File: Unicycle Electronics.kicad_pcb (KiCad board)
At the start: 2 copper layers, 100 x 95 mm, 28 parts, among them J1 12V Input, J10 USB_C, J2 Tail Light, J3 BT1, J4 BT2, J5 BT3, J6 UART, J7 Tail Light, Q1 AO3402, SW1 PTS526SMG15SMTR2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

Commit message: PCB Revision 1
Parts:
- J7: value Tail Light -> Headlight
- moved J7 96.2 mm to (102.2, 122.5), turned to 90 degrees
- moved Q1 76.9 mm to (171.0, 41.5)
- moved C4 72.0 mm to (150.5, 41.0), turned to 90 degrees
- moved C2 66.4 mm to (148.0, 41.0), turned to 90 degrees
- moved C1 64.4 mm to (144.0, 41.5)
- moved J5 52.7 mm to (178.1, 67.0), turned to 90 degrees
- moved C3 49.6 mm to (146.5, 63.5), turned to 90 degrees
- moved R4 49.6 mm to (160.5, 117.5), turned to 180 degrees
- moved SW2 49.3 mm to (154.0, 60.0), turned to 180 degrees
- moved SW1 35.9 mm to (154.0, 67.0), turned to 180 degrees
- moved R8 33.9 mm to (160.5, 114.0)
- moved U3 33.2 mm to (145.5, 48.5)
- moved J10 31.4 mm to (174.2, 123.8)
- moved R3 31.0 mm to (170.0, 47.0), turned to 90 degrees
- moved J2 29.1 mm to (176.5, 41.0), turned to -90 degrees
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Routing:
- net +12V: track 0.00 -> 153.0 mm
- net GND: track 0.00 -> 112.2 mm, vias 0 -> 7
- net /DIM-: track 0.00 -> 96.2 mm
- net /USB-: track 0.00 -> 79.1 mm, vias 0 -> 2
- net /USB+: track 0.00 -> 76.4 mm, vias 0 -> 2
- net Net-(LED DRIVER1-PWM): track 0.00 -> 74.9 mm, vias 0 -> 2
- net +3.3V: track 0.00 -> 56.1 mm
- net /Head_Dimming: track 0.00 -> 41.1 mm, vias 0 -> 2
- net /BT1: track 0.00 -> 36.1 mm
- net /BOOT: track 0.00 -> 31.3 mm
- net /BT2: track 0.00 -> 29.1 mm
- net Net-(J7-Pin_2): track 0.00 -> 28.8 mm
- net Net-(U2-EN/CHIP_PU): track 0.00 -> 26.9 mm
- net /BT3: track 0.00 -> 22.8 mm
- net /RXD0: track 0.00 -> 17.8 mm
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- added copper zone on B.Cu, net GND

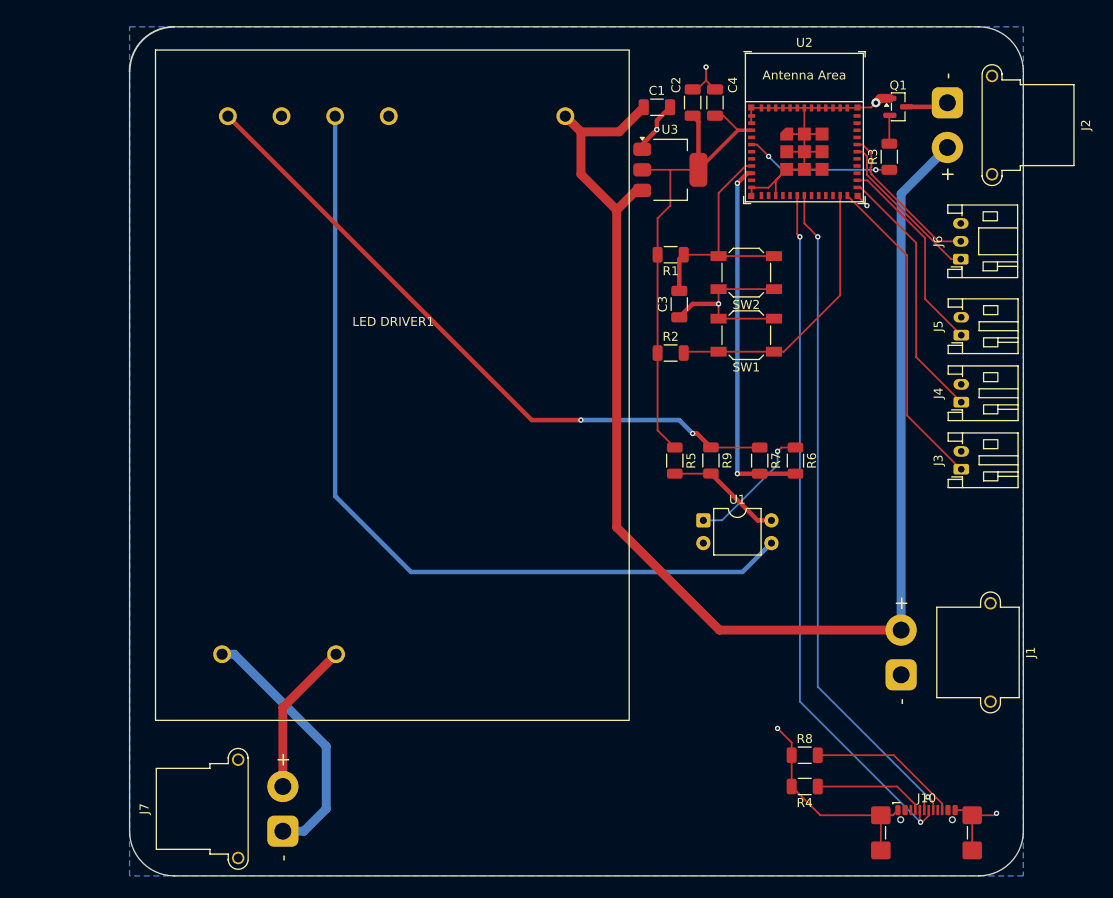
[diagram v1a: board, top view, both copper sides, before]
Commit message: Added mounting holes, updated footprints
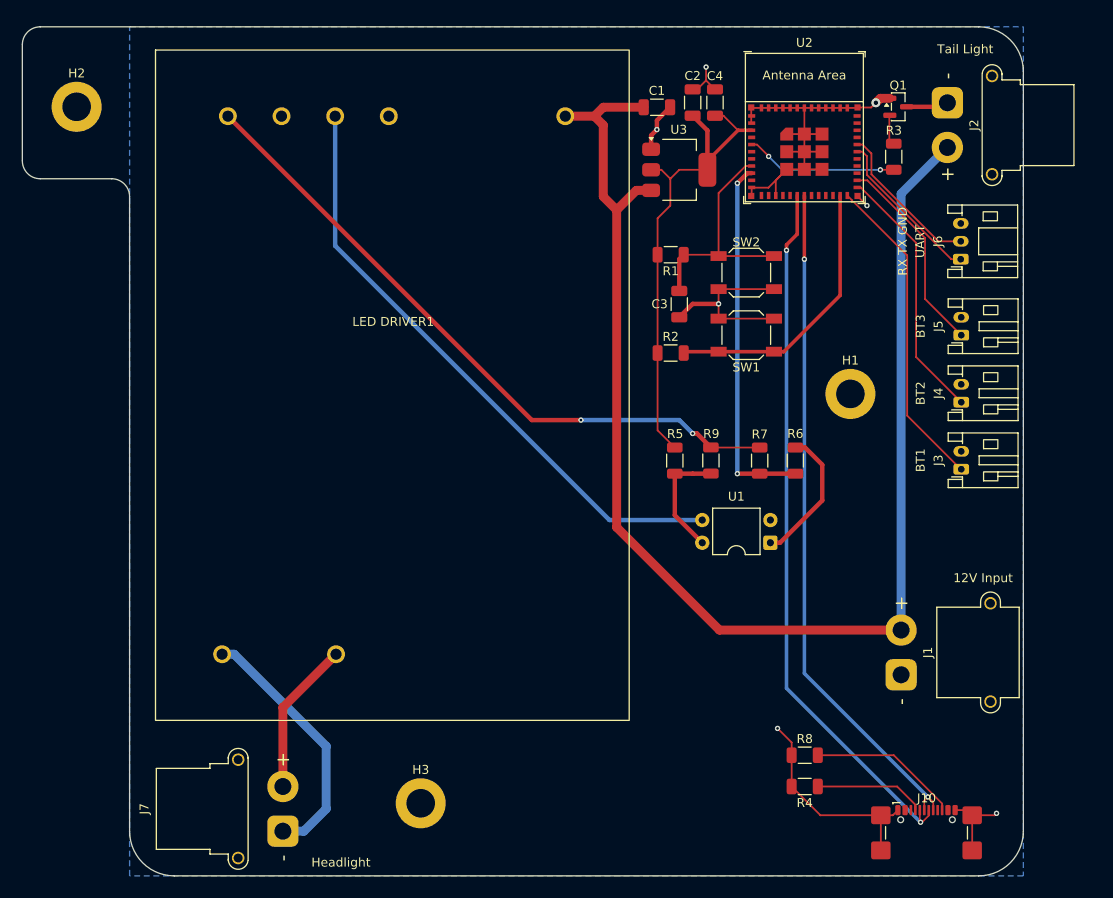
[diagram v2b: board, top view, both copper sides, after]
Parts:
- added H1: MountingHole, MountingHole:MountingHole_3.2mm_M3_DIN965_Pad, F.Cu at (165.7, 73.6)
- added H2: MountingHole, MountingHole:MountingHole_3.2mm_M3_DIN965_Pad, F.Cu at (79.1, 41.5)
- added H3: MountingHole, MountingHole:MountingHole_3.2mm_M3_DIN965_Pad, F.Cu at (117.6, 119.4)
- moved U1 7.91 mm to (156.7, 90.2), turned to 180 degrees
- moved U3 1.00 mm to (146.5, 48.5)
- moved R3 0.50 mm to (170.5, 47.0)
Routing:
- net /DIM-: track 96.2 -> 68.3 mm
- net Net-(R6-Pad1): track 14.6 -> 15.6 mm, vias 1 -> 0
- net /USB-: track 79.1 -> 80.1 mm
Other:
- board size 100 x 95 mm -> 112 x 95 mm
- board text added: "RX TX GND"

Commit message: pre mfg
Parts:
- moved H3 0.69 mm to (117.0, 119.0)
- moved H1 0.55 mm to (166.0, 74.0)
- moved H2 0.46 mm to (79.0, 41.0)
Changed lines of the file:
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@@
 	(footprint "MountingHole:MountingHole_3.2mm_M3_DIN965_Pad"
 		(layer "F.Cu")
-		(at 79.075 41.45)
+		(at 79 41)
 		(descr "Mounting Hole 3.2mm, M3, generated by kicad-footprint-generator mountinghole.py")
 		(tags "mountinghole M3 DIN965")
@@
 		(tags "resistor")
 		(property "Reference" "R7"
-			(at -2.943337 -0.00819 180)
+			(at -2.943337 -0.00819 0)
 			(layer "F.SilkS")
 			(effects
@@
 		(sheetname "/")
 		(sheetfile "Unicycle Electronics.kicad_sch")
-		(attr smd)
+		(attr smd dnp)
 		(fp_line
 			(start -0.727064 0.91)
@@
 	(footprint "MountingHole:MountingHole_3.2mm_M3_DIN965_Pad"
 		(layer "F.Cu")
-		(at 165.65 73.575)
+		(at 166 74)
 		(descr "Mounting Hole 3.2mm, M3, generated by kicad-footprint-generator mountinghole.py")
 		(tags "mountinghole M3 DIN965")
@@
 	(footprint "MountingHole:MountingHole_3.2mm_M3_DIN965_Pad"
 		(layer "F.Cu")
-		(at 117.575 119.375)
+		(at 117 119)
 		(descr "Mounting Hole 3.2mm, M3, generated by kicad-footprint-generator mountinghole.py")
 		(tags "mountinghole M3 DIN965")
@@
 		(polygon
 			(pts
-				(xy 85 32.5) (xy 185 32.5) (xy 185 127.5) (xy 85 127.5)
+				(xy 84.5 50) (xy 72.5 50) (xy 72.5 31.5) (xy 185 31.5) (xy 185 128) (xy 84.5 128)
 			)
 		)

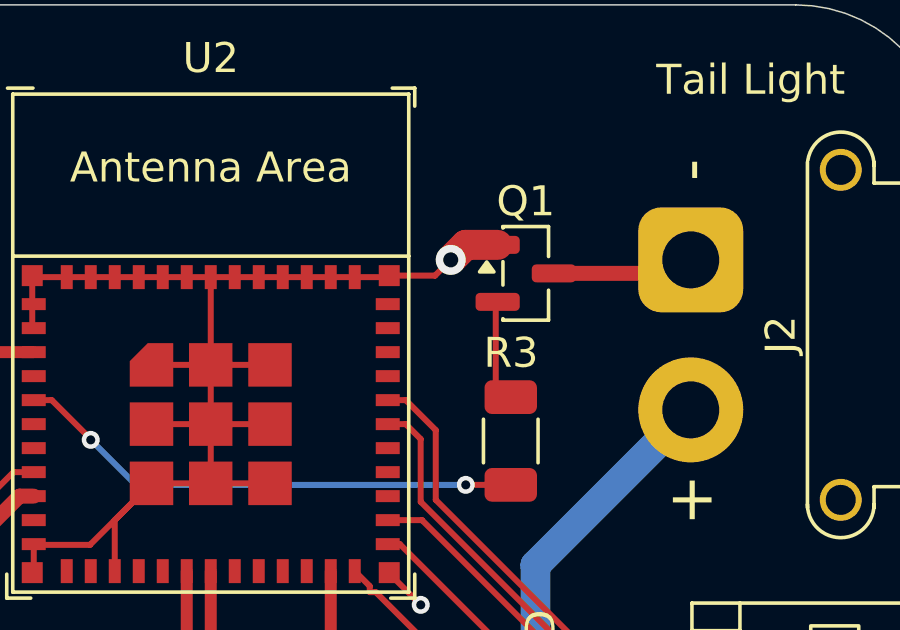
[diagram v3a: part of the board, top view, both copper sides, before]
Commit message: Fixed footprint and routing for tail light MOSFET
gate and source were switched, incorrect footprint :(
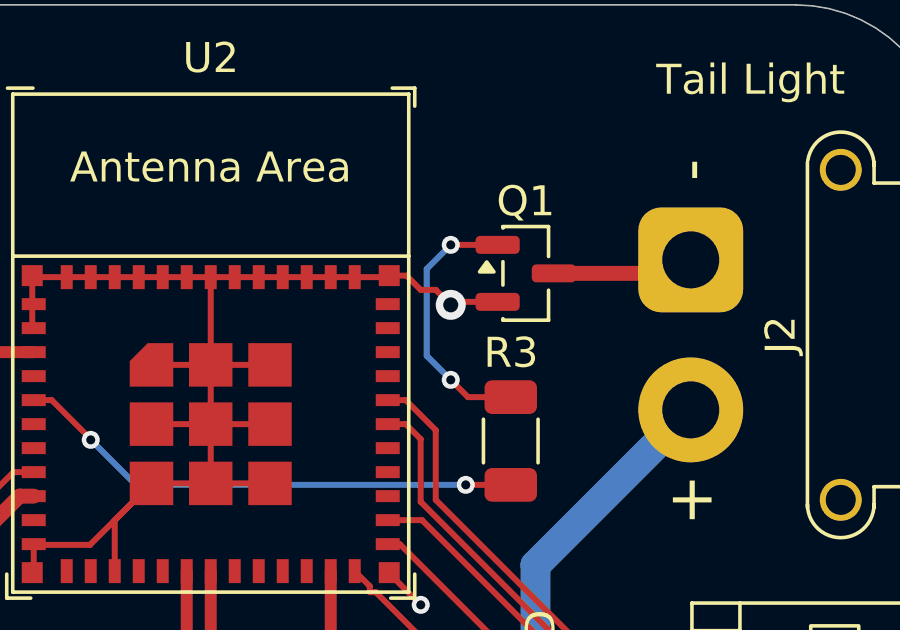
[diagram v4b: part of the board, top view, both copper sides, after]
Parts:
- Q1: footprint Package_TO_SOT_SMD:SOT-23 -> Unicycle:AO3402
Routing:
- net Net-(Q1-G): track 3.20 -> 8.96 mm, vias 0 -> 2
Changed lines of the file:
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@@
 		(sheetname "/")
 		(sheetfile "Unicycle Electronics.kicad_sch")
-		(attr smd dnp)
+		(attr smd)
 		(fp_line
 			(start -0.727064 0.91)
@@
 		)
 	)
-	(footprint "Package_TO_SOT_SMD:SOT-23"
+	(footprint "Unicycle:AO3402"
 		(layer "F.Cu")
 		(at 171 41.45)
@@
 		)
 		(pad "1" smd roundrect
-			(at -0.9375 -0.95)
+			(at -0.9375 0.95)
 			(size 1.475 0.6)
 			(layers "F.Cu" "F.Mask" "F.Paste")
@@
 		)
 		(pad "2" smd roundrect
-			(at -0.9375 0.95)
+			(at -0.9375 -0.95)
 			(size 1.475 0.6)
 			(layers "F.Cu" "F.Mask" "F.Paste")
@@
 	)
 	(segment
-		(start 170.0625 40.5)
-		(end 169 40.5)
-		(width 1)
-		(layer "F.Cu")
-		(net 1)
-	)
-	(segment
 		(start 162.29322 120.71822)
 		(end 169.05541 120.71822)
@@
 	)
 	(segment
-		(start 168.5 41)
-		(end 167.975 41.525)
+		(start 160.5 44.5)
+		(end 162.475 44.5)
 		(width 0.2)
 		(layer "F.Cu")
@@
 	)
 	(segment
-		(start 160.5 44.5)
-		(end 162.475 44.5)
+		(start 179.27541 124.64822)
+		(end 179.27541 120.71822)
 		(width 0.2)
 		(layer "F.Cu")
@@
 	)
 	(segment
-		(start 179.27541 124.64822)
-		(end 179.27541 120.71822)
+		(start 167.025 41.525)
+		(end 166.45 41.525)
 		(width 0.2)
 		(layer "F.Cu")
@@
 	)
 	(segment
-		(start 167.975 41.525)
-		(end 166.45 41.525)
-		(width 0.2)
-		(layer "F.Cu")
-		(net 1)
-	)
-	(segment
 		(start 160.5 46.475)
 		(end 160.5 48.45)
@@
 	)
 	(segment
+		(start 167.5 42)
+		(end 167.025 41.525)
+		(width 0.2)
+		(layer "F.Cu")
+		(net 1)
+	)
+	(segment
 		(start 148 63.5)
 		(end 150.9 63.5)
@@
 	)
 	(segment
-		(start 169 40.5)
-		(end 168.5 41)
-		(width 1)
-		(layer "F.Cu")
-		(net 1)
-	)
-	(segment
 		(start 154.55 43.225)
 		(end 154.6 43.275)
@@
 	)
 	(segment
+		(start 170.0625 42.4)
+		(end 168.6 42.4)
+		(width 0.2)
+		(layer "F.Cu")
+		(net 1)
+	)
+	(segment
 		(start 178.70041 120.14322)
 		(end 179.27541 120.71822)
@@
 	)
 	(segment
+		(start 170.0625 42.4)
+		(end 170 42.4625)
+		(width 0.2)
+		(layer "F.Cu")
+		(net 1)
+	)
+	(segment
 		(start 160.5 48.45)
 		(end 162.475 48.45)
@@
 	)
 	(segment
+		(start 168.5 42.5)
+		(end 168 42)
+		(width 0.2)
+		(layer "F.Cu")
+		(net 1)
+	)
+	(segment
+		(start 168.6 42.4)
+		(end 168.5 42.5)
+		(width 0.2)
+		(layer "F.Cu")
+		(net 1)
+	)
+	(segment
+		(start 168 42)
+		(end 167.5 42)
+		(width 0.2)
+		(layer "F.Cu")
+		(net 1)
+	)
+	(segment
 		(start 154.625 50.5)
 		(end 156.475 50.5)
@@
 	)
 	(via
-		(at 168.5 41)
+		(at 168.5 42.5)
 		(size 1)
 		(drill 0.5)
@@
 	)
 	(segment
-		(start 170.0625 42.4)
-		(end 170 42.4625)
+		(start 170.5 45.575)
+		(end 169.075 45.575)
+		(width 0.2)
+		(layer "F.Cu")
+		(net 19)
+	)
+	(segment
+		(start 168.5 40.5)
+		(end 170.0625 40.5)
 		(width 0.2)
 		(layer "F.Cu")
@@
 	)
 	(segment
-		(start 170 42.4625)
-		(end 170 45.575)
+		(start 169.075 45.575)
+		(end 168.5 45)
 		(width 0.2)
 		(layer "F.Cu")
 		(net 19)
 	)
+	(via
+		(at 168.5 40.5)
+		(size 0.6)
+		(drill 0.3)
+		(layers "F.Cu" "B.Cu")
+		(net 19)
+	)
+	(via
+		(at 168.5 45)
+		(size 0.6)
+		(drill 0.3)
+		(layers "F.Cu" "B.Cu")
+		(net 19)
+	)
+	(segment
+		(start 168.5 45)
+		(end 167.699 44.199)
+		(width 0.2)
+		(layer "B.Cu")
+		(net 19)
+	)
+	(segment
+		(start 167.699 44.199)
+		(end 167.699 41.301)
+		(width 0.2)
+		(layer "B.Cu")
+		(net 19)
+	)
+	(segment
+		(start 167.699 41.301)
+		(end 168.5 40.5)
+		(width 0.2)
+		(layer "B.Cu")
+		(net 19)
+	)

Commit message: updated 3d models
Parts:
- J1: footprint Connector_AMASS:AMASS_XT30PW-M_1x02_P2.50mm_Horizontal -> Unicycle:AMASS_XT30PW-M_1x02_P2.50mm_Horizontal
- J2, J7: footprint Connector_AMASS:AMASS_XT30PW-F_1x02_P2.50mm_Horizontal -> Unicycle:AMASS_XT30PW-F_1x02_P2.50mm_Horizontal
